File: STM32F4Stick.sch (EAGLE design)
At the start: 35 parts, among them U1 MIC5219 3.3V

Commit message: Board layout is almost complete. Needs extension header pins and silkscreen stuff.
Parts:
- removed D4: RED, SparkFun-LED:LED-RED0603
- added D3: RED, SparkFun-LED:LED-RED0603
- added JP4: (no value), SparkFun-Connectors:M03PTH
- C1: value 2.2uF -> 1.0uF; device SparkFun-Capacitors:2.2UF-10V-20%(0603) -> SparkFun-Capacitors:1.0UF-16V-10%(0603)
- C10: value 2.2uF -> 0.1uF; device SparkFun-Capacitors:CAP_POL1206 -> SparkFun-Capacitors:0.1UF-25V-5%(0603)
- C12: value 1.0uF -> 4.7uF; device SparkFun-Capacitors:1.0UF-16V-10%(0603) -> SparkFun-Capacitors:CAP_POL1206
- C13, C6: value 0.1uF -> 2.2uF; device SparkFun-Capacitors:0.1UF-25V-5%(0603) -> SparkFun-Capacitors:2.2UF-10V-20%(0603)
- C14: value 4.7uF -> 0.1uF; device SparkFun-Capacitors:CAP_POL1206 -> SparkFun-Capacitors:0.1UF-25V-5%(0603)
- C2: value 2.2uF -> 0.1uF; device SparkFun-Capacitors:2.2UF-10V-20%(0603) -> SparkFun-Capacitors:0.1UF-25V-5%(0603)
- C3: value 0.1uF -> 2.2uF; device SparkFun-Capacitors:0.1UF-25V-5%(0603) -> SparkFun-Capacitors:CAP_POL1206
- C4, C5: value 0.1uF -> 12pF; device SparkFun-Capacitors:0.1UF-25V-5%(0603) -> SparkFun-Capacitors:12PF-50V-5%(0603)
- C8, C9: value 12pF -> 0.1uF; device SparkFun-Capacitors:12PF-50V-5%(0603) -> SparkFun-Capacitors:0.1UF-25V-5%(0603)
- D1: value BLUE -> GREEN; device SparkFun-LED:LED-BLUE0603 -> SparkFun-LED:LED-GREEN0603
- D2: value GREEN -> BLUE; device SparkFun-LED:LED-GREEN0603 -> SparkFun-LED:LED-BLUE0603
- JP2: value M15 -> (none); device SparkFun-Connectors:M15 -> SparkFun-Connectors:M03PTH
- JP3: value (none) -> M15; device SparkFun-Connectors:M03PTH -> SparkFun-Connectors:M15
- R3, R6: value 10K -> 1K; device SparkFun-Resistors:10KOHM1/10W1%(0603)0603 -> SparkFun-Resistors:1KOHM1/10W1%(0603)
- R4, R5: value 1K -> 10K; device SparkFun-Resistors:1KOHM1/10W1%(0603) -> SparkFun-Resistors:10KOHM1/10W1%(0603)0603
- renumbered FRAME2 to FRAME1, U$1 to -2, U$2 to -1, U$3 to -16MHZ1
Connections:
- removed net N$33: JP2.2
- removed net N$34: JP2.1
- removed net N$39: D4.C, R7.2
- removed net N$40: D1.C, R4.2
- removed net N$41: D1.A
- removed net N$42: D4.A
- new net 5V: C1.1, JP2.2, JP3.1, U1.EN, U1.IN
- new net LED_BLUE: -2.PA0, R6.2
- new net LED_RED: -2.PA1, R7.2
- net BOOT0: now also R4.2; no longer R3.2
- net BOOT1: now also R5.2, S2.1; no longer R6.2, S1.1
- net GND: now also C10.2, C12.-, C14.2, C3.-, D1.C, D2.C, D3.C, JP1.2, JP2.1, JP3.2, JP4.3, R5.1, S1.2; no longer C10.-, C12.2, C14.-, C3.2, JP3.3, R3.1, R5.2, R6.1, R7.1, S2.2
- net N$1: now also C6.1; no longer C1.1
- net N$10: now also C13.1; no longer C2.1
- net N$18: now also D2.A, R6.1; no longer JP1.2
- net N$19: now also D3.A, R7.1; no longer JP1.1
- net N$20: now also JP3.15; no longer JP2.15
- net N$21: now also JP3.14; no longer JP2.14
- net N$22: now also JP3.13; no longer JP2.13
- net N$23: now also JP3.12; no longer JP2.12
- net N$24: now also JP3.11; no longer JP2.11
- net N$25: now also JP3.10; no longer JP2.10
- net N$26: now also JP3.9; no longer JP2.9
- net N$27: now also JP3.8; no longer JP2.8
- net N$28: now also JP3.7; no longer JP2.7
- net N$29: now also JP3.6; no longer JP2.6
- net N$3: now also C4.1; no longer C9.1
- net N$30: now also JP3.5; no longer JP2.5
- net N$31: now also JP3.4; no longer JP2.4
- net N$32: now also JP3.3; no longer JP2.3
- net N$35: now also D1.A, R3.2; no longer D2.C, R5.1
- net N$4: now also C5.1; no longer C8.1
- net NRST: now also C14.1, S1.1; no longer C3.1, S2.1
- net SWDCK: now also JP4.2; no longer JP3.2
- net SWDIO: now also JP4.1; no longer JP3.1
- net USB_VBUS: now also JP2.3; no longer C12.1, U1.EN, U1.IN
- net VCC: now also C10.1, C12.+, C2.1, C3.+, C8.1, C9.1, JP1.1, R3.1, S2.2; no longer C10.+, C13.1, C14.+, C4.1, C5.1, C6.1, D2.A, S1.2
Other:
- moved on the sheet: C1, C11, C13, C2, C4, C5, C6, C7, C8, C9, D1, D2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

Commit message: Extension header additions to schematic. Routing is complete on the board. The second extension header connections needs to be added.
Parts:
- removed JP4: (no value), SparkFun-Connectors:M03PTH
- JP1, JP3: value M15 -> M161X16_NO_SILK; device SparkFun-Connectors:M15 -> SparkFun-Connectors:M161X16_NO_SILK
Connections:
- removed net N$11: JP1.9
- removed net N$12: JP1.8
- removed net N$13: JP1.7
- removed net N$14: JP1.6
- removed net N$15: JP1.5
- removed net N$16: JP1.4
- removed net N$17: JP1.3
- removed net N$2: JP1.15
- removed net N$5: JP1.14
- removed net N$6: JP1.13
- removed net N$7: JP1.12
- removed net N$8: JP1.11
- removed net N$9: JP1.10
- new net P50: -2.PA15/JTDI, JP1.5
- new net P51: -2.PC10/SDIO_D2, JP1.6
- new net P52: -2.PC11/SDIO_D3, JP1.7
- new net P53: -2.PC12/SDIO_CLK, JP1.8
- new net P54: -2.PD2/SDIO_CMD, JP1.9
- new net P55: -2.PB3/JTDO, JP1.10
- new net P56: -2.PB4/JTRST, JP1.11
- new net P57: -2.PB5, JP1.12
- new net P58: -2.PB6, JP1.13
- new net P59: -2.PB7, JP1.14
- new net P61: -2.PB8, JP1.15
- new net P62: -2.PB9, JP1.16
- new net USB_ID: -2.PA10/UART1_RX
- net GND: no longer JP4.3
- net SWDCK: now also JP1.4; no longer JP4.2
- net SWDIO: now also JP1.3; no longer JP4.1
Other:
- note removed: "3-pin programming header"

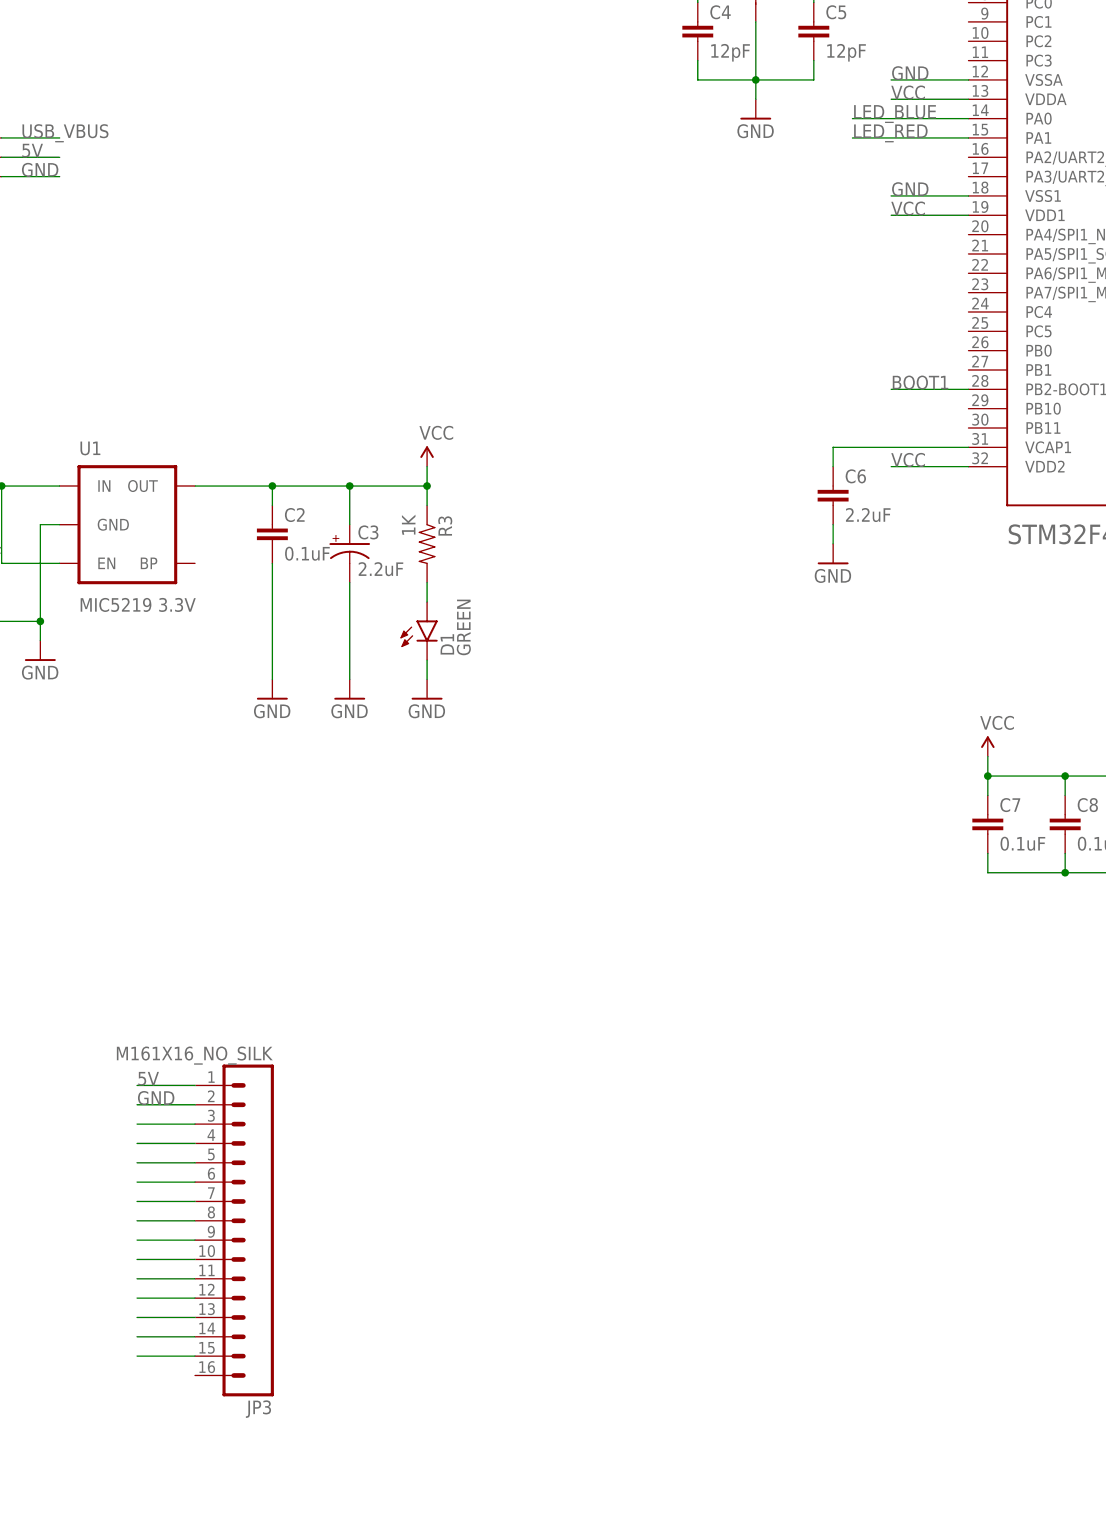
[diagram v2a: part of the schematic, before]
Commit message: Added SD-Card. Still need to route the extension pins.
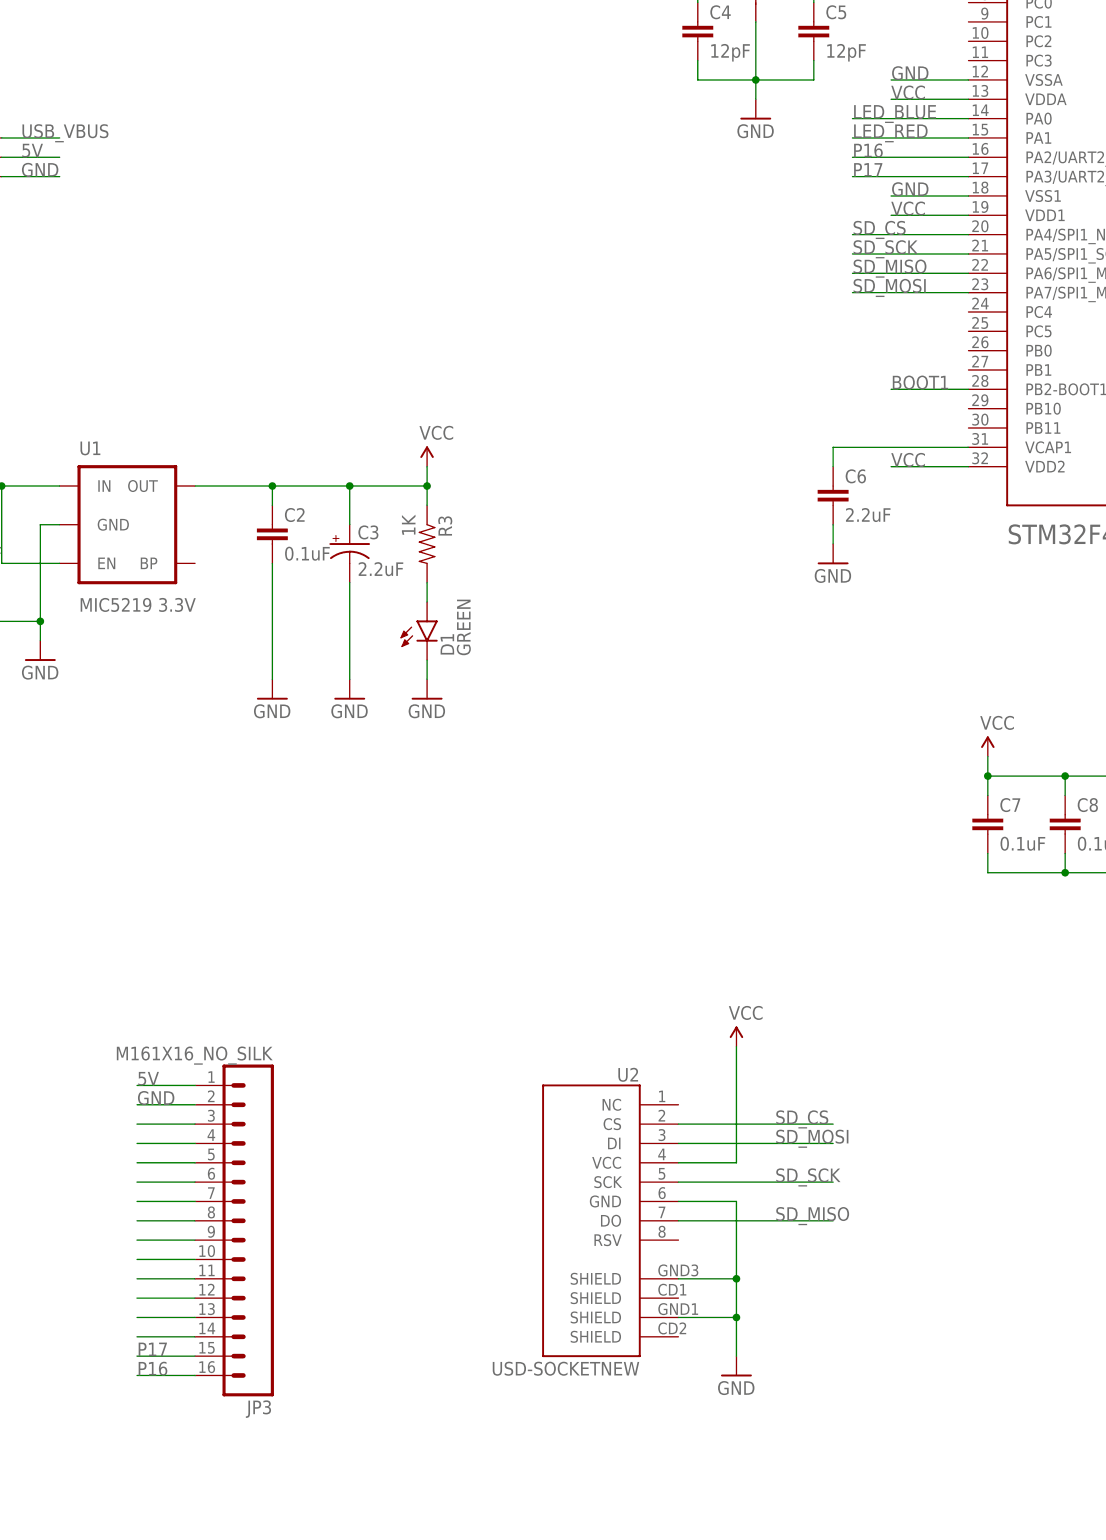
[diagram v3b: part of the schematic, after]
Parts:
- added U2: USD-SOCKETNEW, SparkFun-Connectors:USD-SOCKETNEW
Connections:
- removed net N$20: JP3.15
- new net P16: -2.PA2/UART2_TX, JP3.16
- new net P17: -2.PA3/UART2_RX, JP3.15
- new net SD_CS: -2.PA4/SPI1_NSS, U2.CS
- new net SD_MISO: -2.PA6/SPI1_MISO, U2.DO
- new net SD_MOSI: -2.PA7/SPI1_MOSI, U2.DI
- new net SD_SCK: -2.PA5/SPI1_SCK, U2.SCK
- net GND: now also U2.GND, U2.SHIELD@1, U2.SHIELD@3
- net VCC: now also U2.VCC
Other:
- note added: "SD/MMC Card"
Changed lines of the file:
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@@
 <part name="D3" library="SparkFun-LED" deviceset="LED-RED" device="0603" value="RED"/>
 <part name="R7" library="SparkFun-Resistors" deviceset="1KOHM1/10W1%(0603)" device="" value="1K"/>
+<part name="U2" library="SparkFun-Connectors" deviceset="USD-SOCKET" device="NEW"/>
+<part name="GND17" library="SparkFun-Aesthetics" deviceset="GND" device=""/>
+<part name="SUPPLY5" library="SparkFun-Aesthetics" deviceset="VCC" device=""/>
 </parts>
 <sheets>
@@
 <text x="124.46" y="233.68" size="1.778" layer="150">16 MHZ</text>
 <text x="116.84" y="236.22" size="1.778" layer="150">Needed for the USB</text>
+<text x="104.14" y="86.36" size="1.778" layer="150">SD/MMC Card</text>
 </plain>
 <instances>
@@
 <instance part="D3" gate="G$1" x="393.7" y="154.94" rot="R90"/>
 <instance part="R7" gate="G$1" x="383.54" y="154.94" rot="R180"/>
+<instance part="U2" gate="G$1" x="114.3" y="66.04" rot="MR0"/>
+<instance part="GND17" gate="1" x="129.54" y="43.18"/>
+<instance part="SUPPLY5" gate="G$1" x="129.54" y="86.36"/>
 </instances>
 <busses>
@@
 <label x="22.86" y="81.28" size="1.778" layer="95"/>
 </segment>
+<segment>
+<pinref part="U2" gate="G$1" pin="VCC"/>
+<wire x1="121.92" y1="71.12" x2="129.54" y2="71.12" width="0.1524" layer="91"/>
+<pinref part="SUPPLY5" gate="G$1" pin="VCC"/>
+<wire x1="129.54" y1="71.12" x2="129.54" y2="86.36" width="0.1524" layer="91"/>
+</segment>
 </net>
 <net name="GND" class="0">
@@
 <label x="50.8" y="78.74" size="1.778" layer="95"/>
 </segment>
+<segment>
+<pinref part="U2" gate="G$1" pin="SHIELD@1"/>
+<wire x1="121.92" y1="55.88" x2="129.54" y2="55.88" width="0.1524" layer="91"/>
+<pinref part="GND17" gate="1" pin="GND"/>
+<wire x1="129.54" y1="55.88" x2="129.54" y2="50.8" width="0.1524" layer="91"/>
+<pinref part="U2" gate="G$1" pin="SHIELD@3"/>
+<wire x1="129.54" y1="50.8" x2="129.54" y2="45.72" width="0.1524" layer="91"/>
+<wire x1="121.92" y1="50.8" x2="129.54" y2="50.8" width="0.1524" layer="91"/>
+<pinref part="U2" gate="G$1" pin="GND"/>
+<wire x1="121.92" y1="66.04" x2="129.54" y2="66.04" width="0.1524" layer="91"/>
+<wire x1="129.54" y1="66.04" x2="129.54" y2="55.88" width="0.1524" layer="91"/>
+<junction x="129.54" y="55.88"/>
+<junction x="129.54" y="50.8"/>
+</segment>
 </net>
 <net name="N$10" class="0">
@@
 </segment>
 </net>
-<net name="N$20" class="0">
+<net name="P17" class="0">
 <segment>
 <pinref part="JP3" gate="G$1" pin="15"/>
 <wire x1="58.42" y1="45.72" x2="50.8" y2="45.72" width="0.1524" layer="91"/>
+<label x="50.8" y="45.72" size="1.778" layer="95"/>
+</segment>
+<segment>
+<pinref part="-2" gate="G$1" pin="PA3/UART2_RX"/>
+<wire x1="160.02" y1="200.66" x2="144.78" y2="200.66" width="0.1524" layer="91"/>
+<label x="144.78" y="200.66" size="1.778" layer="95"/>
 </segment>
 </net>
@@
 </segment>
 </net>
+<net name="SD_CS" class="0">
+<segment>
+<pinref part="-2" gate="G$1" pin="PA4/SPI1_NSS"/>
+<wire x1="160.02" y1="193.04" x2="144.78" y2="193.04" width="0.1524" layer="91"/>
+<label x="144.78" y="193.04" size="1.778" layer="95"/>
+</segment>
+<segment>
+<pinref part="U2" gate="G$1" pin="CS"/>
+<wire x1="121.92" y1="76.2" x2="142.24" y2="76.2" width="0.1524" layer="91"/>
+<label x="134.62" y="76.2" size="1.778" layer="95"/>
+</segment>
+</net>
+<net name="SD_SCK" class="0">
+<segment>
+<pinref part="-2" gate="G$1" pin="PA5/SPI1_SCK"/>
+<wire x1="160.02" y1="190.5" x2="144.78" y2="190.5" width="0.1524" layer="91"/>
+<label x="144.78" y="190.5" size="1.778" layer="95"/>
+</segment>
+<segment>
+<pinref part="U2" gate="G$1" pin="SCK"/>
+<wire x1="121.92" y1="68.58" x2="142.24" y2="68.58" width="0.1524" layer="91"/>
+<label x="134.62" y="68.58" size="1.778" layer="95"/>
+</segment>
+</net>
+<net name="SD_MISO" class="0">
+<segment>
+<pinref part="-2" gate="G$1" pin="PA6/SPI1_MISO"/>
+<wire x1="160.02" y1="187.96" x2="144.78" y2="187.96" width="0.1524" layer="91"/>
+<label x="144.78" y="187.96" size="1.778" layer="95"/>
+</segment>
+<segment>
+<pinref part="U2" gate="G$1" pin="DO"/>
+<wire x1="121.92" y1="63.5" x2="142.24" y2="63.5" width="0.1524" layer="91"/>
+<label x="134.62" y="63.5" size="1.778" layer="95"/>
+</segment>
+</net>
+<net name="SD_MOSI" class="0">
+<segment>
+<pinref part="-2" gate="G$1" pin="PA7/SPI1_MOSI"/>
+<wire x1="160.02" y1="185.42" x2="144.78" y2="185.42" width="0.1524" layer="91"/>
+<label x="144.78" y="185.42" size="1.778" layer="95"/>
+</segment>
+<segment>
+<pinref part="U2" gate="G$1" pin="DI"/>
+<wire x1="121.92" y1="73.66" x2="142.24" y2="73.66" width="0.1524" layer="91"/>
+<label x="134.62" y="73.66" size="1.778" layer="95"/>
+</segment>
+</net>
+<net name="P16" class="0">
+<segment>
+<pinref part="JP3" gate="G$1" pin="16"/>
+<wire x1="58.42" y1="43.18" x2="50.8" y2="43.18" width="0.1524" layer="91"/>
+<label x="50.8" y="43.18" size="1.778" layer="95"/>
+</segment>
+<segment>
+<pinref part="-2" gate="G$1" pin="PA2/UART2_TX"/>
+<wire x1="160.02" y1="203.2" x2="144.78" y2="203.2" width="0.1524" layer="91"/>
+<label x="144.78" y="203.2" size="1.778" layer="95"/>
+</segment>
+</net>

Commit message: Finished Schematic / Board layout. Silkscreen needs to be added
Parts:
- removed -16MHZ1: CRYSTAL-GROUNDED, SparkFun-FreqCtrl:CRYSTAL-GROUNDED
- added Q1: (no value), adafruit:XTAL-4-3225
- added R10, R11, R8, R9: 100k, SparkFun-Resistors:100KOHM1/10W1%(0603)
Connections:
- removed net N$21: JP3.14
- removed net N$22: JP3.13
- removed net N$23: JP3.12
- removed net N$24: JP3.11
- removed net N$25: JP3.10
- removed net N$26: JP3.9
- removed net N$27: JP3.8
- removed net N$28: JP3.7
- removed net N$29: JP3.6
- removed net N$30: JP3.5
- removed net N$31: JP3.4
- removed net N$32: JP3.3
- new net P26: -2.PB0, JP3.14
- new net P27: -2.PB1, JP3.13
- new net P29: -2.PB10, JP3.12
- new net P30: -2.PB11, JP3.11, R9.1
- new net P33: -2.PB12/I2S2_WS, JP3.10
- new net P34: -2.PB13/I2S2_CK, JP3.9
- new net P35: -2.PB14/I2S2_XD, JP3.8
- new net P36: -2.PB15/I2S2_SD, JP3.7
- new net P37: -2.PC6/I2S2_MCK, JP3.6
- new net P39: -2.PC8/SDIO_D0, JP3.5
- new net P40: -2.PC9/SDIO_D1, JP3.4
- new net P41: -2.PA8, JP3.3
- net GND: now also Q1.G1, Q1.G2; no longer -16MHZ1.3
- net N$3: now also Q1.X1; no longer -16MHZ1.1
- net N$4: now also Q1.X2; no longer -16MHZ1.2
- net P52: now also R10.1
- net P57: now also R11.1
- net USB_ID: now also R8.1
- net VCC: now also R10.2, R11.2, R8.2, R9.2
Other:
- note added: "PA10 (USB_ID) is pulled high"
- note added: "PA10, PB5, PB11, PC11 needs stable"
- note added: "PB11 (P30) is pulled high"
- note added: "PB5 (P57) is pulled high"
- note added: "PC11 (P52) is pulled high"
- note added: "levels for USB bootloader"
- moved on the sheet: C13, C4, C5

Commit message: Final version for Rev A.
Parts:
- added C15: 0.1uF, SparkFun-Capacitors:0.1UF-25V-5%(0603)
- added LOGO1: OSHW-LOGOM, SparkFun-Aesthetics:OSHW-LOGOM
- C5: value 12pF -> 2.2uF; device SparkFun-Capacitors:12PF-50V-5%(0603) -> SparkFun-Capacitors:2.2UF-10V-20%(0603)
- C6: value 2.2uF -> 12pF; device SparkFun-Capacitors:2.2UF-10V-20%(0603) -> SparkFun-Capacitors:12PF-50V-5%(0603)
- JP2: device SparkFun-Connectors:M03PTH -> SparkFun-Connectors:M031X03_NO_SILK
- R10, R11: value 100k -> 1K; device SparkFun-Resistors:100KOHM1/10W1%(0603) -> SparkFun-Resistors:1KOHM1/10W1%(0603)
- R4, R5: value 10K -> 100k; device SparkFun-Resistors:10KOHM1/10W1%(0603)0603 -> SparkFun-Resistors:100KOHM1/10W1%(0603)
- R6, R7: value 1K -> 100k; device SparkFun-Resistors:1KOHM1/10W1%(0603) -> SparkFun-Resistors:100KOHM1/10W1%(0603)
- R8, R9: value 100k -> 10K; device SparkFun-Resistors:100KOHM1/10W1%(0603) -> SparkFun-Resistors:10KOHM1/10W1%(0603)0603
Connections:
- new net N$2: C15.1, U1.BP
- net BOOT0: now also R8.2; no longer R4.2
- net BOOT1: now also R9.2; no longer R5.2
- net GND: now also C15.2, R8.1, R9.1; no longer R4.1, R5.1
- net LED_BLUE: now also R10.2; no longer R6.2
- net LED_RED: now also R11.2; no longer R7.2
- net N$1: now also C5.1; no longer C6.1
- net N$18: now also R10.1; no longer R6.1
- net N$19: now also R11.1; no longer R7.1
- net N$4: now also C6.1; no longer C5.1
- net P30: now also R5.1; no longer R9.1
- net P52: now also R7.1; no longer R10.1
- net P57: now also R6.1; no longer R11.1
- net USB_ID: now also R4.1; no longer R8.1
- net VCC: now also R4.2, R5.2, R6.2, R7.2; no longer R10.2, R11.2, R8.2, R9.2
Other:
- note added: "5V to 3.3V Voltage regulator (LDO)"
- note added: "Decoupling capacitors for the STM32F405 chip Place one cap per VDD pin"
- note added: "External power / USB Power select Put a jumper between pins 2-3 for USB power"
- note added: "PA10, PB5, PB11, PC11 needs stable levels for USB bootloader PA10 (USB_ID) is pulled high PB11 (P30) is pulled high PB5 (P57) is pulled high PC11 (P52) is pulled high"
- note added: "SD/MMC Card in SPI Mode"
- note added: "Short SJ1 to put the chip into bootloader mode when powered on"
- note added: "USB can be used for programming through bootloader It requires an external oscillator to be hooked up"
- note removed: "5V to 3.3V Voltage regulator"
- note removed: "Decoupling capacitors"
- note removed: "It requires an external oscillator to be hooked up"
- note removed: "PA10 (USB_ID) is pulled high"
- note removed: "PA10, PB5, PB11, PC11 needs stable"
- note removed: "PB11 (P30) is pulled high"
- note removed: "PB5 (P57) is pulled high"
- note removed: "PC11 (P52) is pulled high"
- note removed: "Place one cap per VDD pin"
- note removed: "SD/MMC Card"
- note removed: "Short SJ1 to put the chip into"
- note removed: "USB can be used for programming through bootloader"
- note removed: "bootloader mode when powered on."
- note removed: "for the STM32F405 chip"
- note removed: "levels for USB bootloader"
- moved on the sheet: C2, C3, C5, C6, D1, JP2, R10, R11, R3, R4, R5, R6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
